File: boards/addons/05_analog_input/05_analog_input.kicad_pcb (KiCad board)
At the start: 2 copper layers, 47 x 72 mm, 3 parts, among them J1 Conn_02x15_Odd_Even

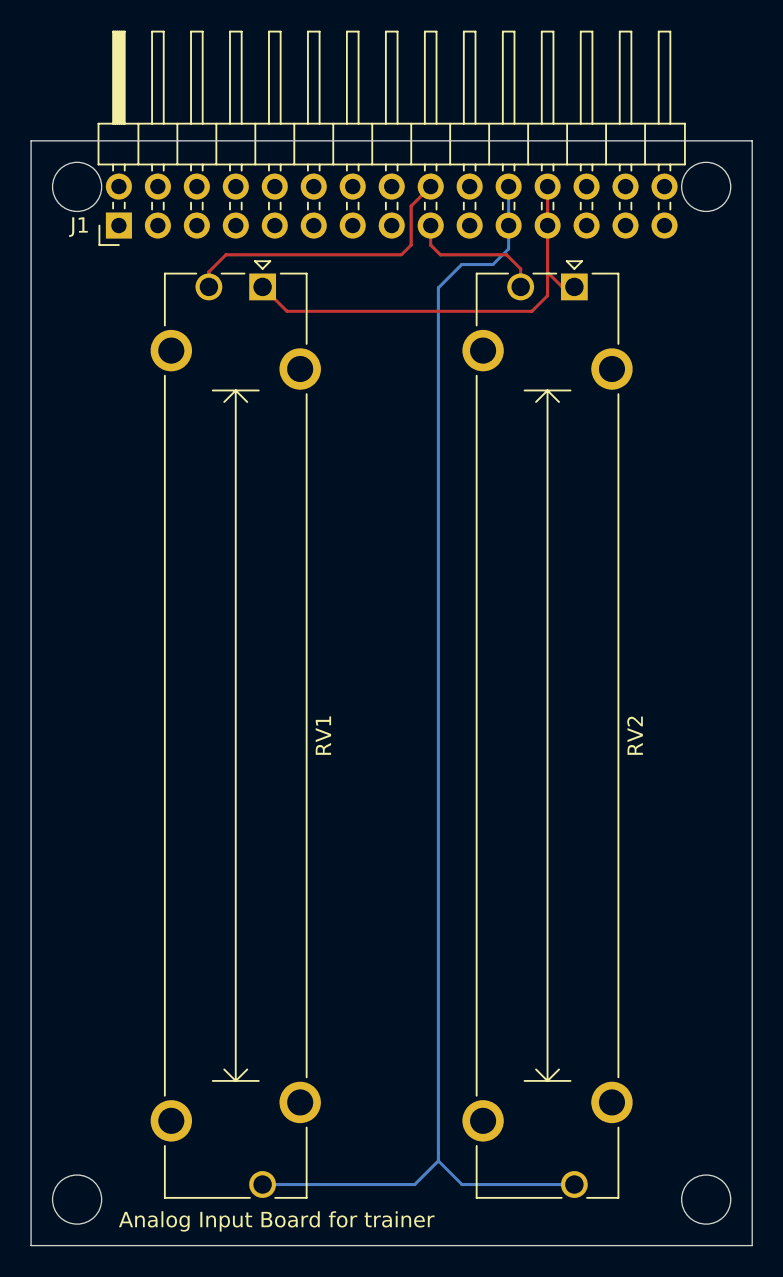
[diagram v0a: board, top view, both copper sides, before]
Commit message: CdS の回路とコンデンサを追加
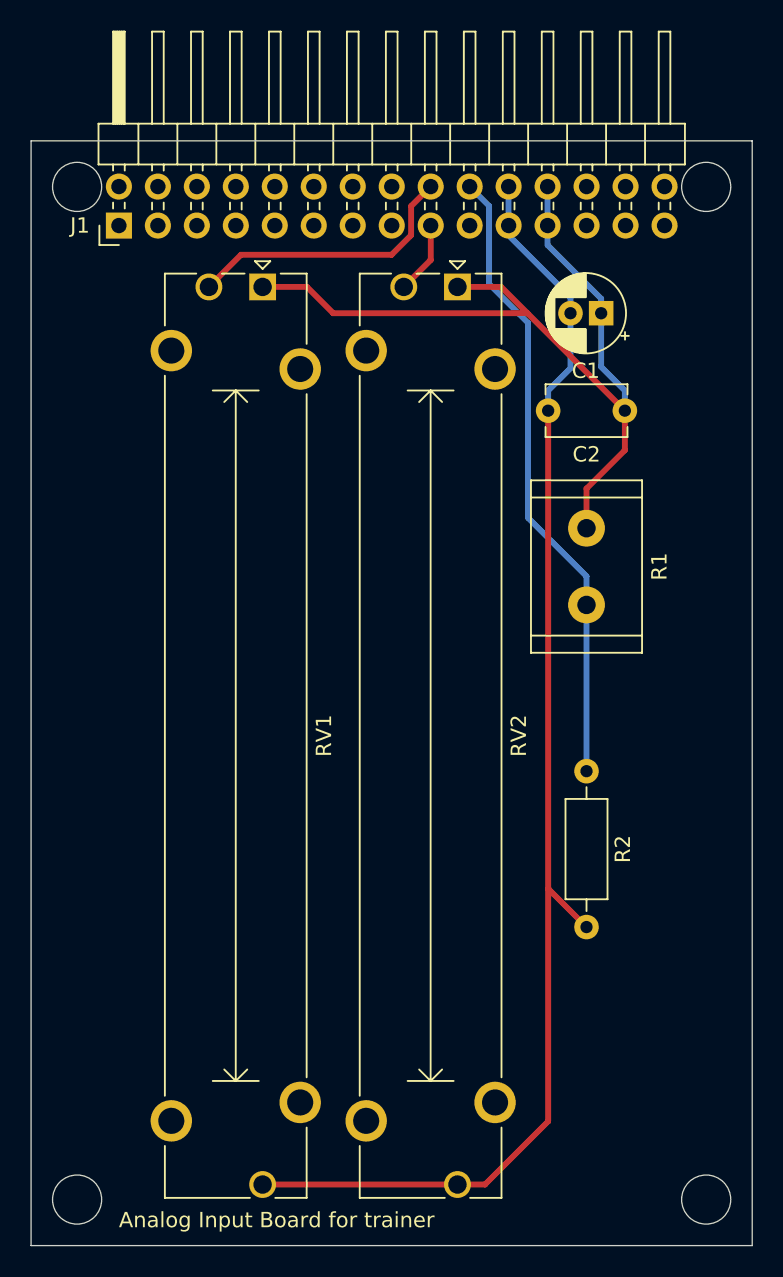
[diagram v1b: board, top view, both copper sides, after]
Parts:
- added C1: 10uF, Capacitor_THT:CP_Radial_D5.0mm_P2.00mm, F.Cu at (166.1, 76.8)
- added C2: 0.1uF, Capacitor_THT:C_Disc_D5.1mm_W3.2mm_P5.00mm, F.Cu at (167.6, 83.2)
- added R1: R, Resistor_THT:R_Radial_Power_L11.0mm_W7.0mm_P5.00mm, F.Cu at (165.1, 90.8)
- added R2: 4.7k, Resistor_THT:R_Axial_DIN0207_L6.3mm_D2.5mm_P10.16mm_Horizontal, F.Cu at (165.1, 106.7)
- moved RV2 7.62 mm to (156.7, 75.1)
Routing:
- net /AD2: track 0.00 -> 41.3 mm
- net +3.3V: track 28.9 -> 57.6 mm
- net /AD1: track 8.96 -> 4.73 mm
- net GND: track 88.2 -> 87.0 mm
- net /AD0: track 19.2 -> 18.3 mm
